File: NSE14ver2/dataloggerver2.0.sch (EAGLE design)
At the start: 26 parts, among them CN1 DM3AT, Q1 16mhz

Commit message: 修正
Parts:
- removed LED4, LED6: (no value), led:LED5MM
- removed R8, R9: 0, rcl:R-US_R0603
- added L1, L2: (no value), Chip LED:OSXX1608C1A
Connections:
- removed net N$3: C3.1, R10.2, SW1.P$2, U$1.PC6RESET
- removed net N$6: BORD1.10, R8.1
- removed net N$9: BORD1.12, R9.1
- new net RESETB: C3.1, JP1.6, R10.2, SW1.P$2, U$1.PC6RESET
- net +3V3: now also BORD1.13, BORD1.8; no longer BORD1.9, R9.2
- net +5V: now also BORD1.10, R10.1; no longer R8.2
- net BORD1: now also BORD1.14, BORD1.7, U$1.PD3; no longer BORD1.15, BORD1.6, U$1.PD2
- net BORD2: now also BORD1.15, BORD1.6, U$1.PD2; no longer BORD1.14, BORD1.7, U$1.PD3
- net GND: now also BORD1.12, BORD1.9, L1.CT, L2.CT; no longer BORD1.13, BORD1.8, LED4.C, LED6.C, R10.1
- net N$1: now also L2.AN; no longer LED6.A
- net N$7: now also L1.AN; no longer LED4.A
- net SS: no longer JP1.6
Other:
- moved on the sheet: BORD1

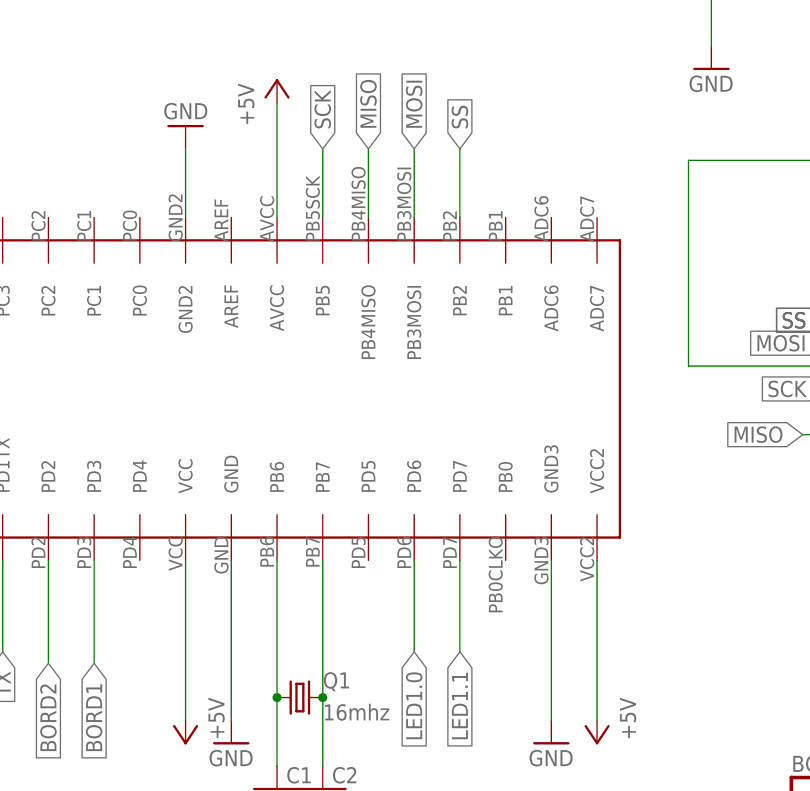
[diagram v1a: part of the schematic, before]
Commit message: 328修正
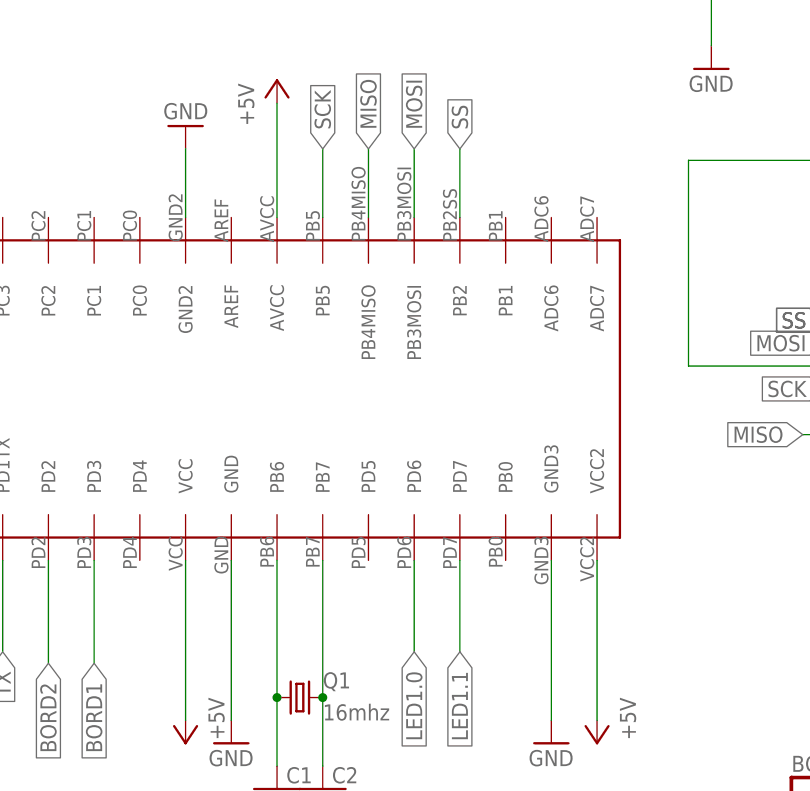
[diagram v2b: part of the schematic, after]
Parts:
- U$1: device ATmega328p-PU:ATMEGA328P-AU -> ATMAGA328P-AU:ATMEGA328P-AU
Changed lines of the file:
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@@
 <setting verticaltext="up"/>
 </settings>
-<grid distance="0.05" unitdist="inch" unit="inch" style="lines" multiple="1" display="no" altdistance="0.01" altunitdist="inch" altunit="inch"/>
+<grid distance="0.1" unitdist="inch" unit="inch" style="lines" multiple="1" display="no" altdistance="0.01" altunitdist="inch" altunit="inch"/>
 <layers>
 <layer number="1" name="Top" color="4" fill="1" visible="no" active="no"/>
@@
 <part name="BORD1" library="pinhead" library_urn="urn:adsk.eagle:library:325" deviceset="PINHD-2X10" device="/90" package3d_urn="urn:adsk.eagle:package:22411/2"/>
 <part name="BORD4" library="pinhead" library_urn="urn:adsk.eagle:library:325" deviceset="PINHD-2X10" device="/90" package3d_urn="urn:adsk.eagle:package:22411/2"/>
-<part name="U$1" library="ATmega328p-PU" deviceset="ATMEGA328P-AU" device="" package3d_urn="urn:adsk.eagle:package:44716433/1"/>
+<part name="U$1" library="ATMAGA328P-AU" deviceset="ATMEGA328P-AU" device="" package3d_urn="urn:adsk.eagle:package:44744060/1"/>
 <part name="R10" library="rcl" library_urn="urn:adsk.eagle:library:334" deviceset="R-US_" device="R0603" package3d_urn="urn:adsk.eagle:package:23555/3" value="10k"/>
 <part name="Q1" library="crystal" library_urn="urn:adsk.eagle:library:204" deviceset="CRYSTAL" device="HC49UP" package3d_urn="urn:adsk.eagle:package:12078/1" value="16mhz"/>
